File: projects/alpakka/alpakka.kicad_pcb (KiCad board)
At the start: 2 copper layers, 130 x 51 mm, 94 parts, among them P1 Debug, P2 Endpoint, P3 Conn_01x02, Q1 Q_PMOS_DGS, U1 Raspberry_Pico, U10 ST_LSM6, U12 ST_LSM6, U2 Alpsalpine_RKJXV, U3 Alpsalpine_EC10E, U4 Alpsalpine_RKJXM, U6 NXP_PCAL6416A, U8 NXP_PCAL6416A

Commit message: Alpakka board RF proto
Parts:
- removed the G*** at (96.6, 80.8)
- removed Q1: Q_PMOS_DGS, ILO_fp:SOT-23-DGS
- removed TP10, TP11, TP12, TP14, TP15, TP16, TP19, TP20, TP24, TP25, TP26, TP3, TP31, TP32, TP33, TP35, TP36, TP4, TP5, TP6, TP7, TP9: Endpoint, ILO_fp:Pad_1mm
- removed the U1 at (100.0, 60.9)
- removed U4: Alpsalpine_RKJXM, ILO_fp:Alpsalpine_RKJXM1015004
- added C3: 100pF, ILO_fp:0402, F.Cu at (124.7, 66.2)
- added C4: 100pF, ILO_fp:0402, F.Cu at (126.1, 66.2)
- added G***: LOGO, LOGO, F.Cu at (90.2, 81.8)
- added G***: LOGO, LOGO, F.Cu at (89.3, 73.5)
- added J1: Conn_01x20_Pin, ILO_fp:Hirose_DF12NB_receptacle, B.Cu at (100.0, 47.0)
- added J2: Conn_01x20_Pin, ILO_fp:Hirose_DF12NB_receptacle, B.Cu at (100.0, 67.0)
- added REF**: NPTH_2mm, ILO_fp:NPTH_2mm, F.Cu at (115.0, 75.0)
- added TPA0: Endpoint, ILO_fp:Pad_1mm, B.Cu at (122.0, 66.5)
- added TPA1: Endpoint, ILO_fp:Pad_1mm, B.Cu at (122.0, 65.1)
- added TPA2: Endpoint, ILO_fp:Pad_1mm, B.Cu at (69.5, 63.0)
- added TPA3: Endpoint, ILO_fp:Pad_1mm, B.Cu at (69.5, 64.8)
- added TPP0: Endpoint, ILO_fp:Pad_1mm, B.Cu at (108.5, 45.0)
- added TPP1: Endpoint, ILO_fp:Pad_1mm, B.Cu at (108.5, 46.5)
- added TPS0: Endpoint, ILO_fp:Pad_1mm, B.Cu at (108.5, 54.5)
- added TPS1: Endpoint, ILO_fp:Pad_1mm, B.Cu at (108.5, 53.0)
- added U2: Alpsalpine_RKJXV, ILO_fp:Alpsalpine_RKJXV122400R, F.Cu at (134.0, 75.0)
- C1, C2: value C -> 100pF
- C5: renamed from C4; value C -> 100pF
- C6: renamed from C3; value C -> 100pF
- C7: renamed from C6; value C -> 100pF
- C8: renamed from C5; value C -> 100pF
- P2: value Endpoint -> Blade
- R1, R2, R3, R4: value R -> 20 Ω
- R6: value R6 -> 2 MΩ
- moved U3 15.0 mm to (112.0, 74.5)
- moved D1 10.0 mm to (100.0, 49.0)
- moved D3 7.07 mm to (100.0, 59.0), turned to 180 degrees
- moved D4 7.07 mm to (95.0, 54.0), turned to 90 degrees
- moved P3 7.00 mm to (70.0, 45.0)
- moved R1 7.00 mm to (100.0, 50.5)
- moved C5 6.50 mm to (38.0, 81.2), turned to -90 degrees
- moved C7 6.50 mm to (156.0, 81.2), turned to -90 degrees
- moved C6 6.50 mm to (44.0, 78.8), turned to -90 degrees
- moved C8 6.50 mm to (162.0, 78.8), turned to -90 degrees
- moved R3 4.95 mm to (100.0, 57.5), turned to 0 degrees
- moved R4 4.95 mm to (96.5, 54.0), turned to -90 degrees
- moved C1 0.35 mm to (74.5, 60.4)
- moved C2 0.30 mm to (74.5, 61.8)
- turned D2 to -90 degrees
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- renumbered U2 to U1
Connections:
- net ADC0 renamed ADC3
- net ADC1 renamed ADC2
- C6 pad 2: VCCA -> VCC
- C8 pad 2: VCCA -> VCC
- D1 pad 2: GP4 -> GP9
- D2 pad 2: GP5 -> GP8
- D3 pad 2: GP3 -> GP7
- D4 pad 2: GP2 -> GP6
- P2 pad 1: GP7 -> GP12
- R6 pad 1: GP6 -> GP13
- R6 pad 2: GP7 -> GP12
- S14 pad 2: GP20 -> GP23
- U10 pad 12: CS0 -> IMU_CS0
- U10 pad 7: GNDA -> GND
- U10 pad 8: VCCA -> VCC
- U12 pad 12: CS1 -> IMU_CS1
- U12 pad 7: GNDA -> GND
- U12 pad 8: VCCA -> VCC
- U3 pad 1: GP9 -> GP10
- U3 pad 2: GP8 -> GP11
- U6 pad 13: GND -> /A11
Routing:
- net VCCA: track 167.5 -> 0.00 mm, vias 4 -> 0
- net GNDA: track 155.4 -> 0.00 mm, vias 4 -> 0
- net IMU_CS1: track 0.00 -> 86.9 mm, vias 0 -> 1
- net CS1: track 86.6 -> 0.00 mm, vias 2 -> 0
- net IMU_CS0: track 0.00 -> 83.6 mm, vias 0 -> 1
- net CS0: track 71.8 -> 0.00 mm, vias 3 -> 0
- net GP12: track 0.00 -> 63.1 mm, vias 0 -> 3
- net ADC1: track 0.00 -> 46.8 mm, vias 0 -> 1
- net ADC0: track 0.00 -> 42.0 mm, vias 0 -> 1
- net GP9: track 49.3 -> 9.24 mm, vias 2 -> 1
- net GP7: track 51.3 -> 11.5 mm, vias 3 -> 1
- net GP8: track 49.1 -> 11.4 mm, vias 2 -> 1
- net GP11: track 0.00 -> 36.9 mm, vias 0 -> 1
- net GP10: track 0.00 -> 34.8 mm, vias 0 -> 1
- net SPI_CK: track 146.7 -> 179.9 mm, vias 1 -> 4
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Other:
- outline, holes or cut-outs redrawn
- board text added: "BY-NC-SA 4.0"
- board text added: "QR CODE HERE"
- board text added: "RF TEST A1"
- board text removed: "1"
- board text removed: "10"
- board text removed: "13"
- board text removed: "14"
- board text removed: "15"
- board text removed: "16"
- board text removed: "17"
- board text removed: "19"
- board text removed: "2"
- board text removed: "20"
- board text removed: "21"
- board text removed: "22"
- board text removed: "24"
- board text removed: "25"
- board text removed: "26"
- board text removed: "27"
- board text removed: "28"
- board text removed: "3"
- board text removed: "30"
- board text removed: "31"
- board text removed: "32"
- board text removed: "33"
- board text removed: "34"
- board text removed: "36"
- board text removed: "37"
- board text removed: "38"
- board text removed: "39"
- board text removed: "4"
- board text removed: "5"
- board text removed: "7"
- board text removed: "8"
- board text removed: "9"
- board text removed: "JLCJLCJLCJLC"
- board text removed: "USB UP"
- board text removed: "b0.90.2"

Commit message: RF test A2
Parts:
- added C11: 1uF, ILO_fp:0402, F.Cu at (78.0, 61.8)
- added C12: 1uF, ILO_fp:0402, F.Cu at (78.0, 60.4)
- C1: renamed from C2; value 100pF -> 100nF
- C2: renamed from C1; value 100pF -> 100nF
- C3: renamed from C4; value 100pF -> 100nF
- C4: renamed from C3; value 100pF -> 100nF
- C5, C6, C7, C8: value 100pF -> 100nF
- P3: renamed from P1; value Debug -> JST PH
- S15: value l1 -> L1
- S16: value r1 -> R1
- S17: value l2 -> L2
- S18: value r2 -> R2
- S19: value l4 -> L4
- S20: value r4 -> R4
- S5: value a -> A
- S6: value b -> B
- S7: value x -> X
- S8: value y -> Y
- moved C1 0.50 mm to (74.0, 61.8)
- moved C2 0.50 mm to (74.0, 60.4)
- moved U3 0.10 mm to (111.9, 74.5), turned to 90 degrees
- turned S14 to 0 degrees
- renumbered J1 to P1, J2 to P2, P2 to P4, P3 to P6
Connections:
- net /A11 renamed A11
- P1 pad 1: VCC -> UART0_TX
- P1 pad 10: UART_TX -> VCC
- P1 pad 11: GP13 -> IMU_CS0
- P1 pad 12: GP12 -> IMU_CS1
- P1 pad 13: GP11 -> GP6
- P1 pad 14: GP10 -> GP7
- P1 pad 15: GP9 -> GP8
- P1 pad 16: GP8 -> GP9
- P1 pad 17: GP7 -> GP10
- P1 pad 18: GP6 -> GP11
- P1 pad 19: IMU_CS1 -> GP12
- P1 pad 2: VCC -> UART0_RX
- P1 pad 20: IMU_CS0 -> GP13
- P1 pad 9: UART_RX -> VCC
- P2 pad 1: I2C_SDA -> ADC3
- P2 pad 10: ADC3 -> UART1_TX
- P2 pad 11: SPI_CK -> GND
- P2 pad 12: SPI_TX -> GND
- P2 pad 13: SPI_RX -> unconnected-(P2-Pin_13-Pad13)
- P2 pad 14: RUN -> unconnected-(P2-Pin_14-Pad14)
- P2 pad 15: GND -> unconnected-(P2-Pin_15-Pad15)
- P2 pad 16: GND -> unconnected-(P2-Pin_16-Pad16)
- P2 pad 17: GND -> RUN
- P2 pad 18: GND -> SPI_RX
- P2 pad 19: GND -> SPI_TX
- P2 pad 2: I2C_SCL -> ADC2
- P2 pad 20: GND -> SPI_CK
- P2 pad 3: GP22 -> ADC1
- P2 pad 4: GP23 -> ADC0
- P2 pad 5: GP24 -> GP25
- P2 pad 6: GP25 -> GP24
- P2 pad 7: ADC0 -> I2C_SCL
- P2 pad 8: ADC1 -> I2C_SDA
- P2 pad 9: ADC2 -> UART1_RX
- P3 pad 1: UART_TX -> UART0_TX
- P3 pad 2: UART_RX -> UART0_RX
- S11 pad 2: A13 -> A10
- S14 pad 2: GP23 -> GP24
- S19 pad 2: A9 -> A8
- TP204 pad 1: A9 -> A8
- U1 pad 10: A12 -> A9
- U1 pad 8: A12 -> A9
- U6 pad 10: unconnected-(U6-P8-Pad10) -> A8
- U6 pad 12: /A10 -> A10
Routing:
- net A11: track 0.00 -> 50.8 mm
- net A10: track 0.00 -> 40.6 mm
- net A9: track 14.6 -> 36.0 mm, vias 1 -> 0
- net A12: track 31.9 -> 50.8 mm
- net A13: track 34.7 -> 50.8 mm
- net A8: track 0.00 -> 14.5 mm, vias 0 -> 1
- net UART_TX: track 11.9 -> 0.00 mm, vias 1 -> 0
- net UART0_TX: track 0.00 -> 11.9 mm, vias 0 -> 1
- net GP23: track 11.6 -> 0.00 mm, vias 1 -> 0
- net GP24: track 0.00 -> 11.1 mm, vias 0 -> 1
- net UART_RX: track 8.31 -> 0.00 mm, vias 1 -> 0
- net UART0_RX: track 0.00 -> 8.31 mm, vias 0 -> 1
- net GND: track 108.1 -> 104.7 mm
- net GP11: track 36.9 -> 34.5 mm
- net B2: track 10.6 -> 12.9 mm
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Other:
- board text added: "NC"
- board text added: "RF TEST A2"
- board text removed: "QR CODE HERE"
- board text removed: "RF TEST A1"

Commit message: RF test A2 final
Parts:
- removed the C1 at (74.0, 61.8)
- removed the C2 at (74.0, 60.4)
- removed the C3 at (126.1, 66.2)
- removed the C4 at (124.7, 66.2)
- moved C5 3.90 mm to (74.1, 61.8), turned to 0 degrees
- moved C6 3.90 mm to (74.1, 60.4), turned to 0 degrees
- moved P3 0.30 mm to (100.0, 40.2)
- renumbered C5 to C1, C6 to C2, C7 to C3, C8 to C4, C11 to C5, C12 to C6
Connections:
- P1 pad 3: GND -> unconnected-(P1-Pin_3-Pad3)
- P1 pad 4: GND -> unconnected-(P1-Pin_4-Pad4)
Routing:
- net GND: track 104.7 -> 96.0 mm
- net ADC1: track 47.6 -> 45.2 mm, vias 1 -> 0
- net ADC0: track 42.4 -> 40.3 mm, vias 1 -> 0
- net ADC2: track 70.8 -> 69.7 mm
- net GP12: track 64.3 -> 65.3 mm
- net ADC3: track 53.2 -> 52.2 mm

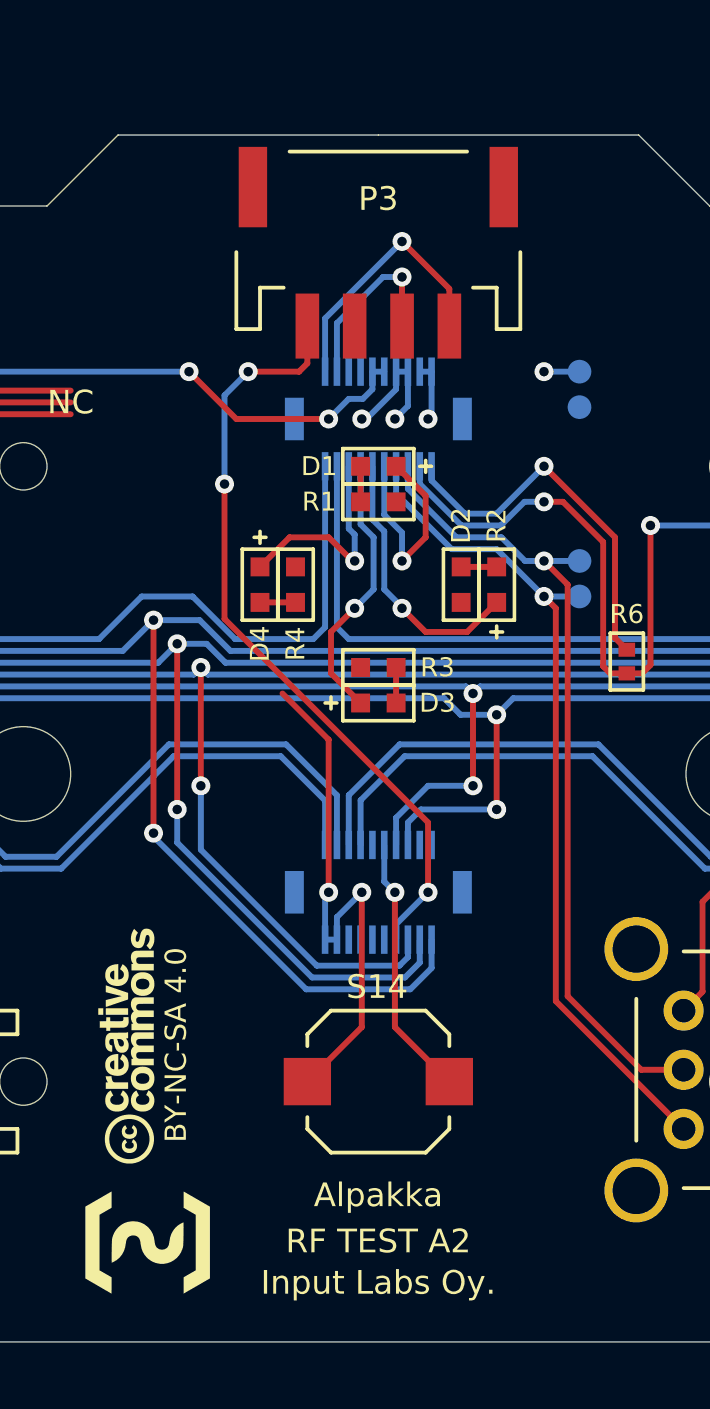
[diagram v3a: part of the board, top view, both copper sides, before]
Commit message: Changed debug port to header pins, Changed nets from global to local
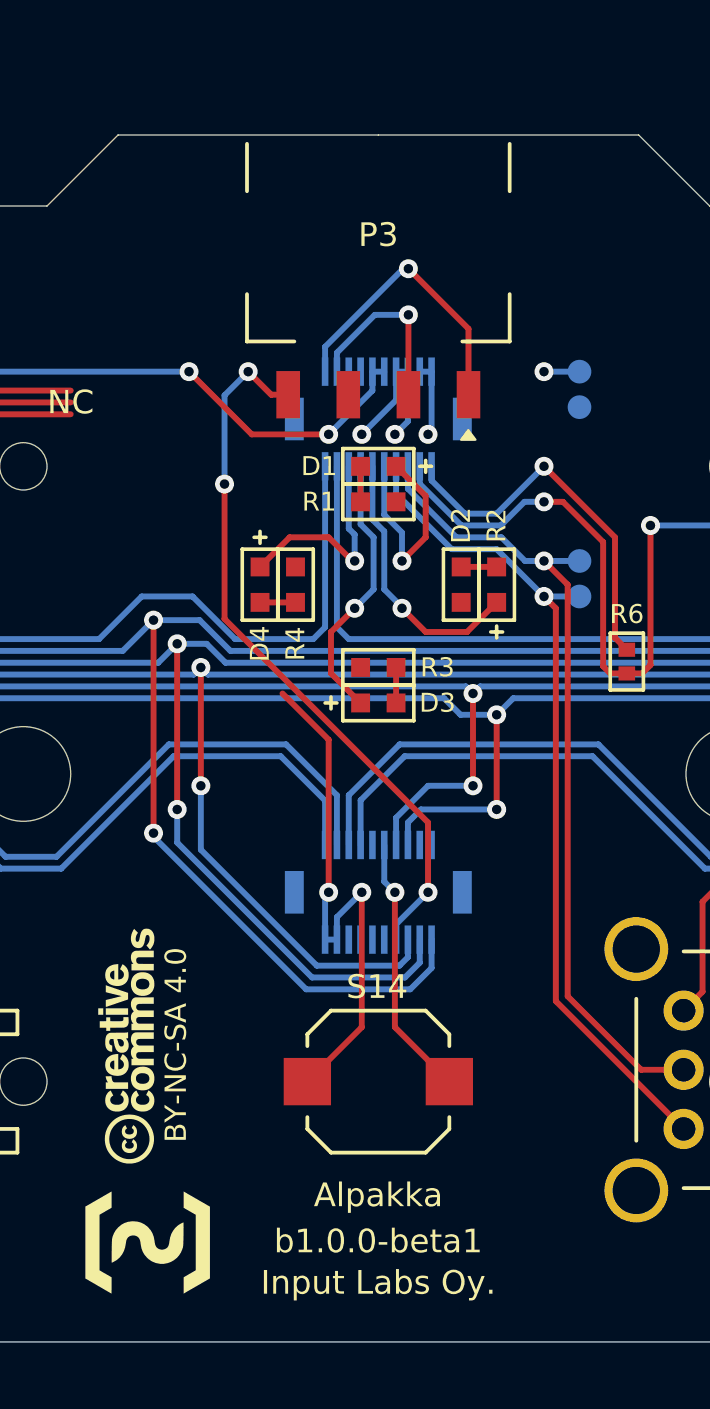
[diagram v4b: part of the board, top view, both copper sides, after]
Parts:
- P3: footprint ILO_fp:JST_S4B-PH-SM4-K-TB -> ILO_fp:XKB_X6511FRS-04
- moved P3 5.77 mm to (100.0, 46.0), turned to 180 degrees
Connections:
- net A0 renamed /A0
- net A1 renamed /A1
- net A10 renamed /A10
- net A11 renamed /A11
- net A12 renamed /A12
- net A13 renamed /A13
- net A14 renamed /A14
- net A15 renamed /A15
- net A2 renamed /A2
- net A3 renamed /A3
- net A4 renamed /A4
- net A8 renamed /A8
- net A9 renamed /A9
- net ADC0 renamed /ADC0
- net ADC1 renamed /ADC1
- net ADC2 renamed /ADC2
- net ADC3 renamed /ADC3
- net B0 renamed /B0
- net B1 renamed /B1
- net B10 renamed /B10
- net B11 renamed /B11
- net B12 renamed /B12
- net B13 renamed /B13
- net B14 renamed /B14
- net B15 renamed /B15
- net B2 renamed /B2
- net B3 renamed /B3
- net B4 renamed /B4
- net B5 renamed /B5
- net B6 renamed /B6
- net B7 renamed /B7
- net BAT renamed /BAT
- net GND renamed /GND
- net GP10 renamed /GP10
- net GP11 renamed /GP11
- net GP12 renamed /GP12
- net GP13 renamed /GP13
- net GP24 renamed /GP24
- net GP25 renamed /GP25
- net GP6 renamed /GP6
- net GP7 renamed /GP7
- net GP8 renamed /GP8
- net GP9 renamed /GP9
- net I2C_SCL renamed /I2C_SCL
- net I2C_SDA renamed /I2C_SDA
- net IMU_CS0 renamed /IMU_CS0
- net IMU_CS1 renamed /IMU_CS1
- net RUN renamed /RUN
- net SPI_CK renamed /SPI_CK
- net SPI_RX renamed /SPI_RX
- net SPI_TX renamed /SPI_TX
- net UART0_RX renamed /UART0_RX
- net UART0_TX renamed /UART0_TX
- net UART1_RX renamed /UART1_RX
- net UART1_TX renamed /UART1_TX
- net VCC renamed /VCC
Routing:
- net /RUN: track 31.8 -> 30.6 mm
- net /GND: track 96.0 -> 97.2 mm
- net /VCC: track 31.3 -> 31.9 mm
- net /BAT: track 31.3 -> 31.9 mm
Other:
- board text added: "b1.0.0-beta1"
- board text removed: "RF TEST A2"

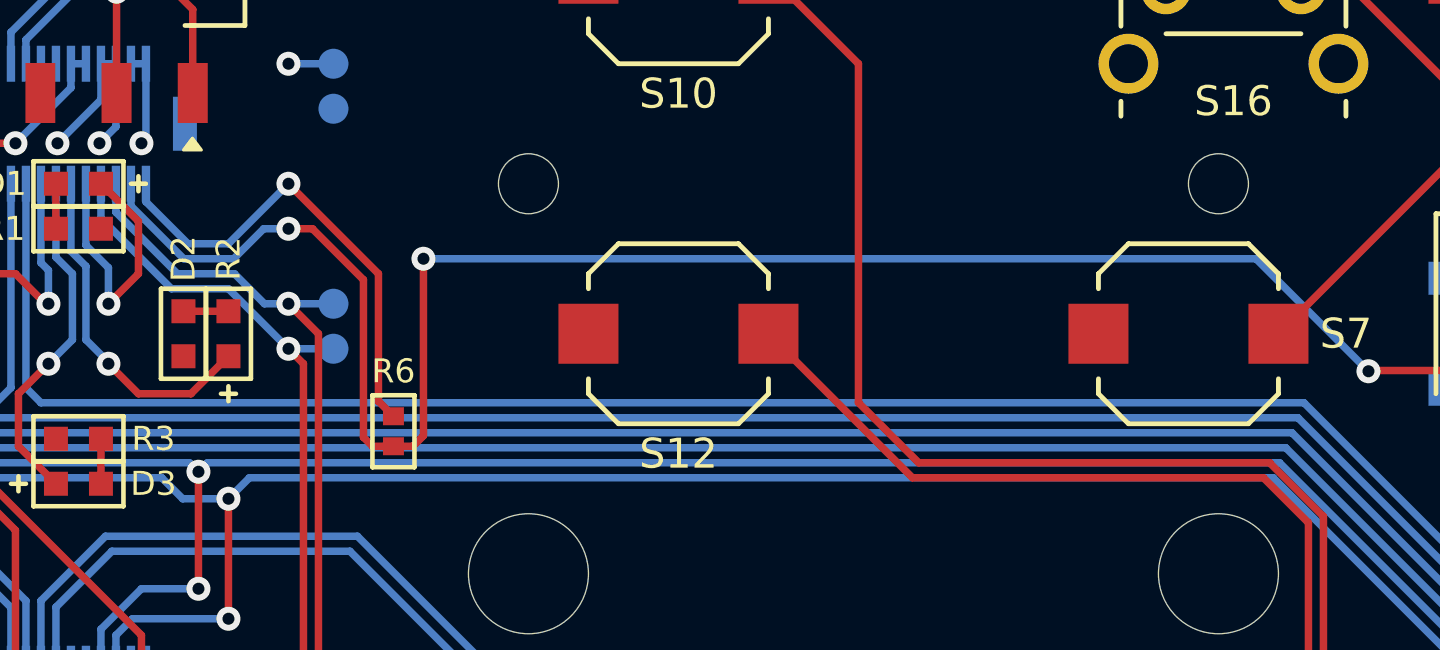
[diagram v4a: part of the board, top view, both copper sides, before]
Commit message: 1M touch resistor with optional 500K mode
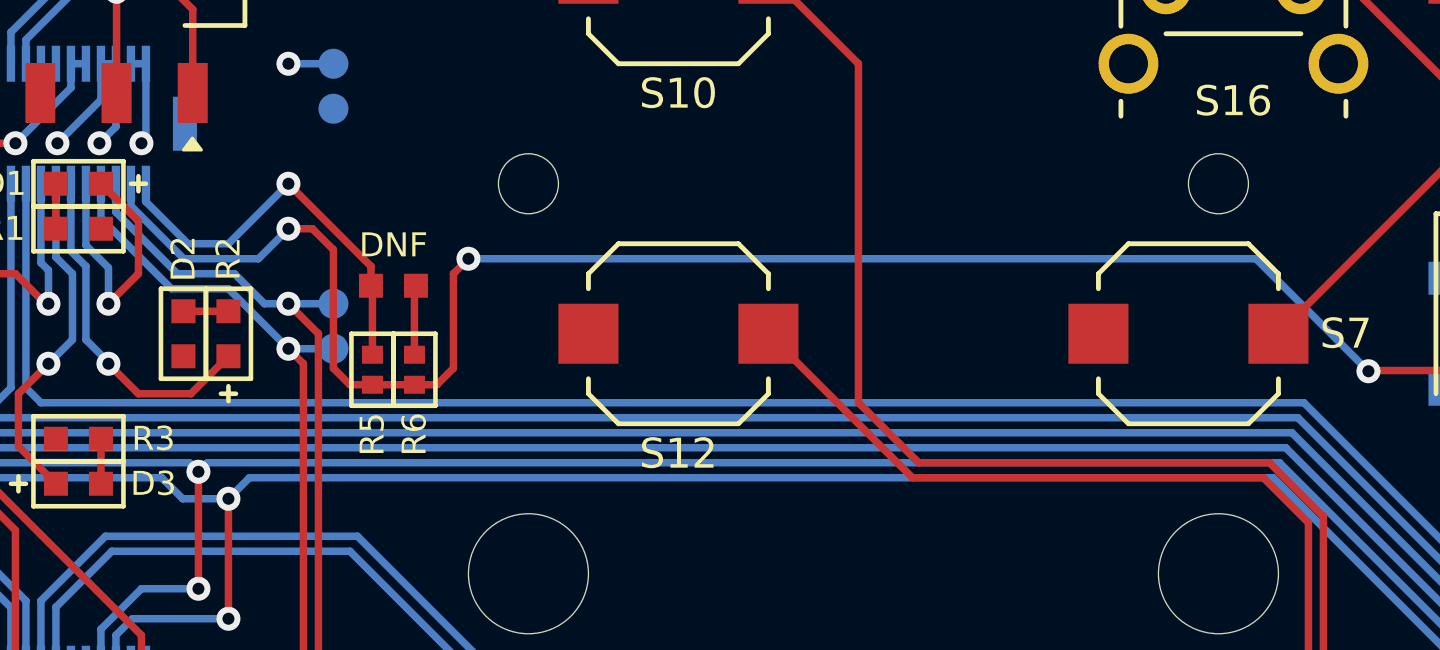
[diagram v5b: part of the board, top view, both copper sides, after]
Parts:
- added R6: 1 MΩ, ILO_fp:0402, F.Cu at (111.2, 55.2)
- added R7: DNP, ILO_fp:0603_compact, F.Cu at (110.5, 52.4)
- P3: value JST PH -> Headers 4P IN
- R5: renamed from R6; value 2 MΩ -> 1 MΩ
- moved R5 2.17 mm to (109.8, 55.2)
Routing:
- net /GP12: track 65.3 -> 61.2 mm
- net /GP13: track 16.0 -> 13.6 mm
- net Net-(R6-Pad1): track 0.00 -> 2.32 mm
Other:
- board text added: "DNF"

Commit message: Battery connector silk placement and 3D model
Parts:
- turned P6 to 0 degrees
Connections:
- P6 pad 1: /BAT -> /GND
- P6 pad 2: /GND -> /BAT
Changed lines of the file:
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@@
 	(footprint "ILO_fp:JST_PH_2_TH"
 		(layer "B.Cu")
-		(at 70 45 180)
+		(at 70 45)
 		(property "Reference" "P6"
-			(at 0 2 0)
+			(at 0 4 0)
 			(unlocked yes)
 			(layer "B.SilkS")
@@
 		)
 		(property "Value" "Conn_01x02"
-			(at 0 6.5 0)
+			(at 0 6.5 180)
 			(unlocked yes)
 			(layer "B.Fab")
@@
 		)
 		(property "Footprint" "ILO_fp:JST_PH_2_TH"
-			(at 0 0 180)
+			(at 0 0 0)
 			(unlocked yes)
 			(layer "F.Fab")
@@
 		)
 		(property "Datasheet" ""
-			(at 0 0 180)
+			(at 0 0 0)
 			(unlocked yes)
 			(layer "F.Fab")
@@
 		)
 		(property "Description" ""
-			(at 0 0 180)
+			(at 0 0 0)
 			(unlocked yes)
 			(layer "F.Fab")
@@
 		)
 		(property "Export" ""
-			(at 0 0 0)
+			(at 0 0 360)
 			(layer "B.Fab")
 			(hide yes)
@@
 		)
 		(property "Mount" ""
-			(at 0 0 0)
+			(at 0 0 360)
 			(layer "B.Fab")
 			(hide yes)
@@
 		)
 		(property "Group" "Batt port"
-			(at 0 0 180)
+			(at 0 0 0)
 			(unlocked yes)
 			(layer "B.Fab")
@@
 		(sheetfile "alpakka.kicad_sch")
 		(attr through_hole)
+		(fp_poly
+			(pts
+				(xy -0.7 -1.65) (xy -1.3 -1.65) (xy -1 -1.25)
+			)
+			(stroke
+				(width 0.1)
+				(type solid)
+			)
+			(fill solid)
+			(layer "B.SilkS")
+		)
+		(fp_poly
+			(pts
+				(xy -3.25 6.55) (xy 3.25 6.55) (xy 3.25 -0.25) (xy 2.25 -0.25) (xy 2.25 1.25) (xy -2.25 1.25) (xy -2.25 -0.25)
+				(xy -3.25 -0.25)
+			)
+			(stroke
+				(width 0.16)
+				(type solid)
+			)
+			(fill none)
+			(layer "B.SilkS")
+		)
 		(fp_text user "${REFERENCE}"
-			(at 0 5 0)
+			(at 0 5 180)
 			(unlocked yes)
 			(layer "B.Fab")
@@
 		)
 		(pad "1" thru_hole circle
-			(at -1 0 180)
+			(at -1 0)
+			(size 1.5 1.5)
+			(drill 0.8)
+			(layers "*.Cu" "*.Mask")
+			(remove_unused_layers no)
+			(net 2 "/GND")
+			(pinfunction "Pin_1")
+			(pintype "passive")
+		)
+		(pad "2" thru_hole circle
+			(at 1 0)
 			(size 1.5 1.5)
 			(drill 0.8)
@@
 			(remove_unused_layers no)
 			(net 17 "/BAT")
-			(pinfunction "Pin_1")
-			(pintype "passive")
-		)
-		(pad "2" thru_hole circle
-			(at 1 0 180)
-			(size 1.5 1.5)
-			(drill 0.8)
-			(layers "*.Cu" "*.Mask")
-			(remove_unused_layers no)
-			(net 2 "/GND")
 			(pinfunction "Pin_2")
 			(pintype "passive")
 		)
+		(model "${KIPRJMOD}/../../symbols/step/JST_PH_2P_90.step"
+			(offset
+				(xyz 0 0 0)
+			)
+			(scale
+				(xyz 1 1 1)
+			)
+			(rotate
+				(xyz 0 0 0)
+			)
+		)
 	)
